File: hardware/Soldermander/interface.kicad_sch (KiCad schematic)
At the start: 10 parts, among them J5 Conn_01x06

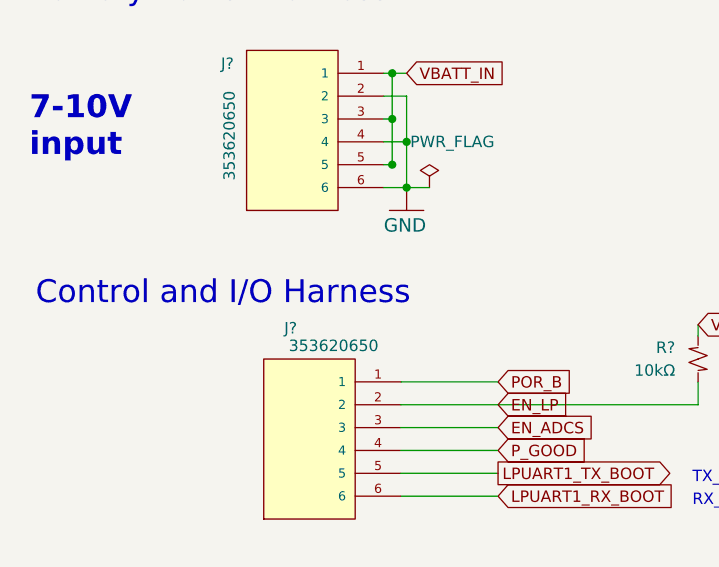
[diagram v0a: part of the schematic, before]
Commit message: update 3.3uH inductor
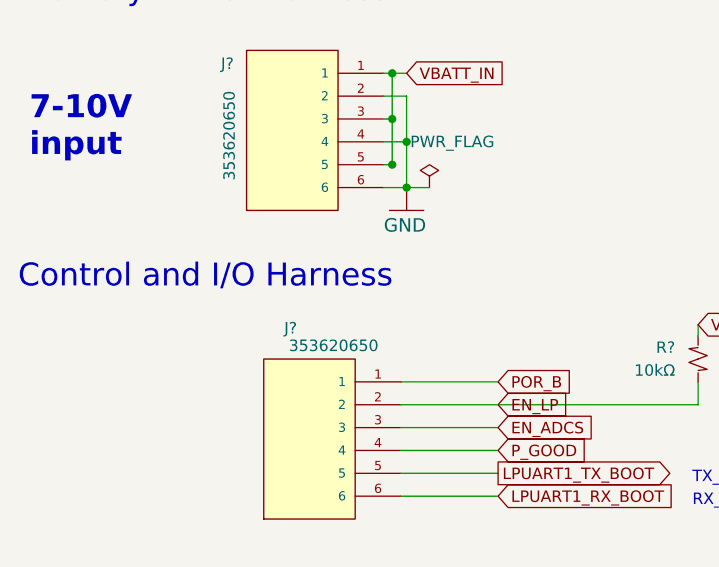
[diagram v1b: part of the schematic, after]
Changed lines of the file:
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@@
     (effects (font (size 1.27 1.27)) (justify left bottom))
   )
-  (text "Control and I/O Harness" (at 157.5308 106.6292 0)
+  (text "Control and I/O Harness" (at 155.575 104.775 0)
     (effects (font (size 2.54 2.54)) (justify left bottom))
   )
@@
     (pin "1")
     (instances
-      (project "cpu_board"
+      (project "Soldermander"
         (path "/c4fd7bdd-408e-44be-b66f-e6a18a0ca6e3/cea27ea3-b252-471b-8ae3-89651d2bf5e1"
           (reference "#GND09") (unit 1)
@@
         )
       )
-      (project "cpu_board"
+      (project "Soldermander"
         (path "/c4fd7bdd-408e-44be-b66f-e6a18a0ca6e3/cea27ea3-b252-471b-8ae3-89651d2bf5e1"
           (reference "#FLG025") (unit 1)
@@
         )
       )
-      (project "cpu_board"
+      (project "Soldermander"
         (path "/c4fd7bdd-408e-44be-b66f-e6a18a0ca6e3/cea27ea3-b252-471b-8ae3-89651d2bf5e1"
           (reference "#PWR062") (unit 1)
@@
     (pin "1")
     (instances
-      (project "cpu_board"
+      (project "Soldermander"
         (path "/c4fd7bdd-408e-44be-b66f-e6a18a0ca6e3/cea27ea3-b252-471b-8ae3-89651d2bf5e1"
           (reference "H1") (unit 1)
@@
     (pin "1")
     (instances
-      (project "cpu_board"
+      (project "Soldermander"
         (path "/c4fd7bdd-408e-44be-b66f-e6a18a0ca6e3/cea27ea3-b252-471b-8ae3-89651d2bf5e1"
           (reference "#PWR063") (unit 1)
@@
     (pin "2")
     (instances
-      (project "cpu_board"
+      (project "Soldermander"
         (path "/c4fd7bdd-408e-44be-b66f-e6a18a0ca6e3/9cbcd73e-afcb-4ff3-8583-4372f7e826ca"
           (reference "R?") (unit 1)
@@
     (pin "1")
     (instances
-      (project "cpu_board"
+      (project "Soldermander"
         (path "/c4fd7bdd-408e-44be-b66f-e6a18a0ca6e3/cea27ea3-b252-471b-8ae3-89651d2bf5e1"
           (reference "H3") (unit 1)
@@
         )
       )
-      (project "cpu_board"
+      (project "Soldermander"
         (path "/c4fd7bdd-408e-44be-b66f-e6a18a0ca6e3/cea27ea3-b252-471b-8ae3-89651d2bf5e1"
           (reference "J2") (unit 1)
@@
         )
       )
-      (project "cpu_board"
+      (project "Soldermander"
         (path "/c4fd7bdd-408e-44be-b66f-e6a18a0ca6e3/cea27ea3-b252-471b-8ae3-89651d2bf5e1"
           (reference "#PWR061") (unit 1)
@@
         )
       )
-      (project "cpu_board"
+      (project "Soldermander"
         (path "/c4fd7bdd-408e-44be-b66f-e6a18a0ca6e3/cea27ea3-b252-471b-8ae3-89651d2bf5e1"
           (reference "J4") (unit 1)
@@
     (pin "1")
     (instances
-      (project "cpu_board"
+      (project "Soldermander"
         (path "/c4fd7bdd-408e-44be-b66f-e6a18a0ca6e3/cea27ea3-b252-471b-8ae3-89651d2bf5e1"
           (reference "H4") (unit 1)
@@
         )
       )
-      (project "cpu_board"
+      (project "Soldermander"
         (path "/c4fd7bdd-408e-44be-b66f-e6a18a0ca6e3/cea27ea3-b252-471b-8ae3-89651d2bf5e1"
           (reference "#GND08") (unit 1)
@@
     (pin "6")
     (instances
-      (project "cpu_board"
+      (project "Soldermander"
         (path "/c4fd7bdd-408e-44be-b66f-e6a18a0ca6e3/cea27ea3-b252-471b-8ae3-89651d2bf5e1"
           (reference "J5") (unit 1)
@@
     (pin "1")
     (instances
-      (project "cpu_board"
+      (project "Soldermander"
         (path "/c4fd7bdd-408e-44be-b66f-e6a18a0ca6e3/cea27ea3-b252-471b-8ae3-89651d2bf5e1"
           (reference "H2") (unit 1)
@@
         )
       )
-      (project "cpu_board"
+      (project "Soldermander"
         (path "/c4fd7bdd-408e-44be-b66f-e6a18a0ca6e3/cea27ea3-b252-471b-8ae3-89651d2bf5e1"
           (reference "J3") (unit 1)
@@
     (pin "2")
     (instances
-      (project "cpu_board"
+      (project "Soldermander"
         (path "/c4fd7bdd-408e-44be-b66f-e6a18a0ca6e3/9cbcd73e-afcb-4ff3-8583-4372f7e826ca"
           (reference "R?") (unit 1)

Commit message: pre-autorouter part 2
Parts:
- R33, R4: renamed from R?; footprint adcs:Perfect_0402 -> Resistor_SMD:R_0402_1005Metric
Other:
- note added: "should I add a pullup of some sort here?"
